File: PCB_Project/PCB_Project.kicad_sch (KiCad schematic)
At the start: 0 parts

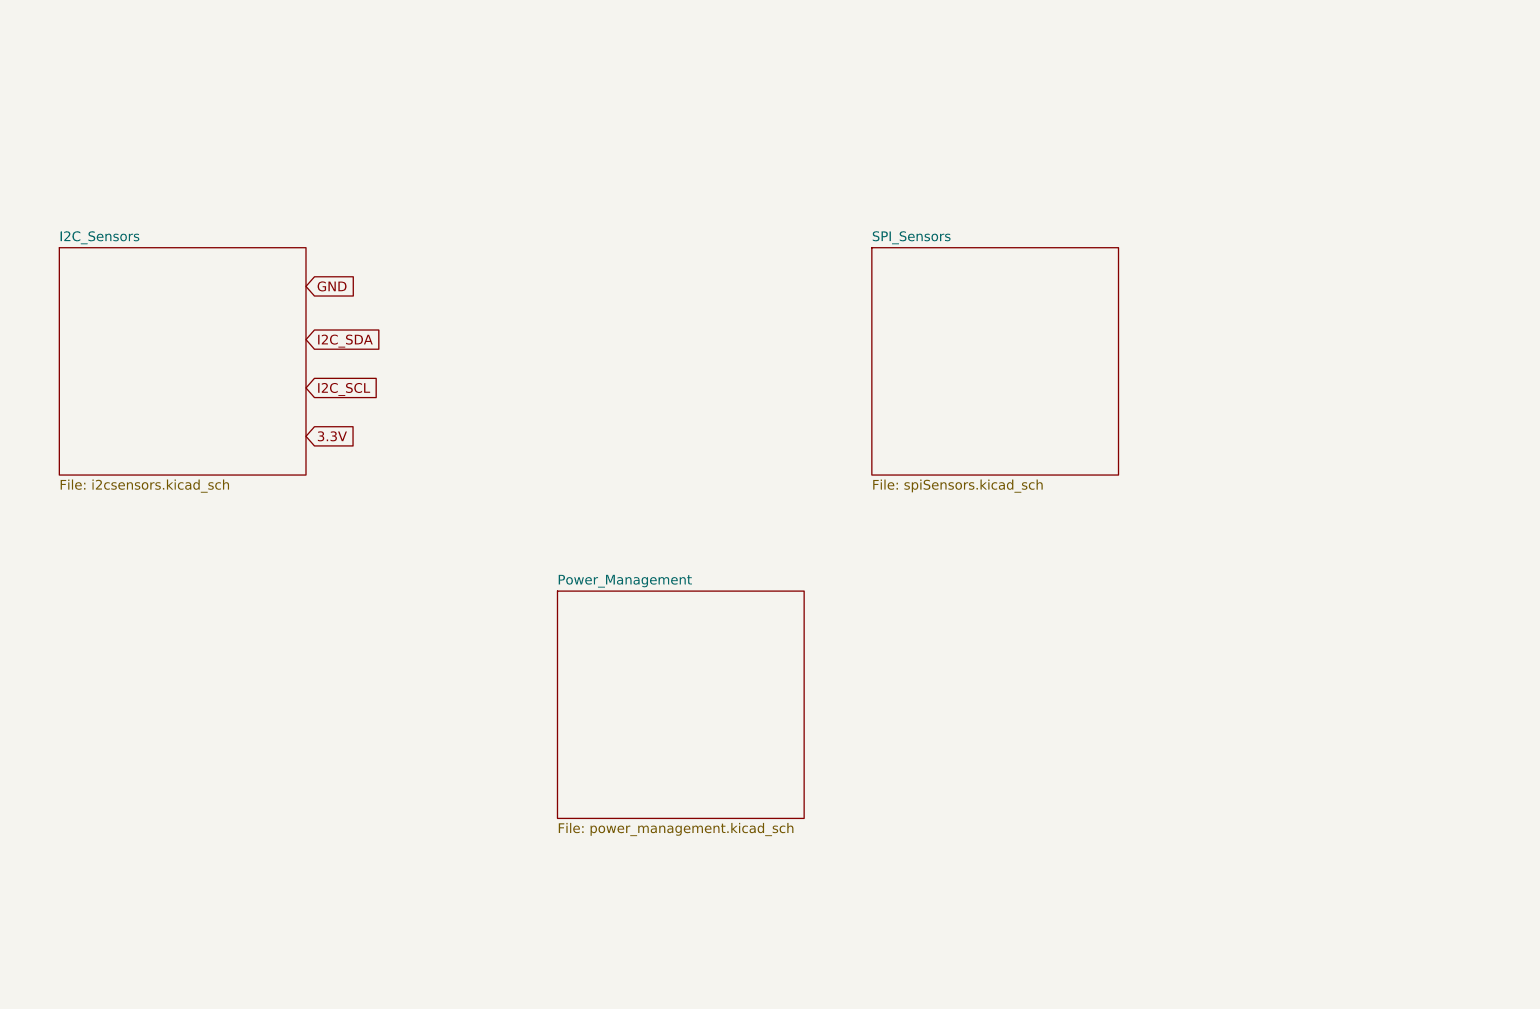
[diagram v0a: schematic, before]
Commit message: added raspberry pi connector
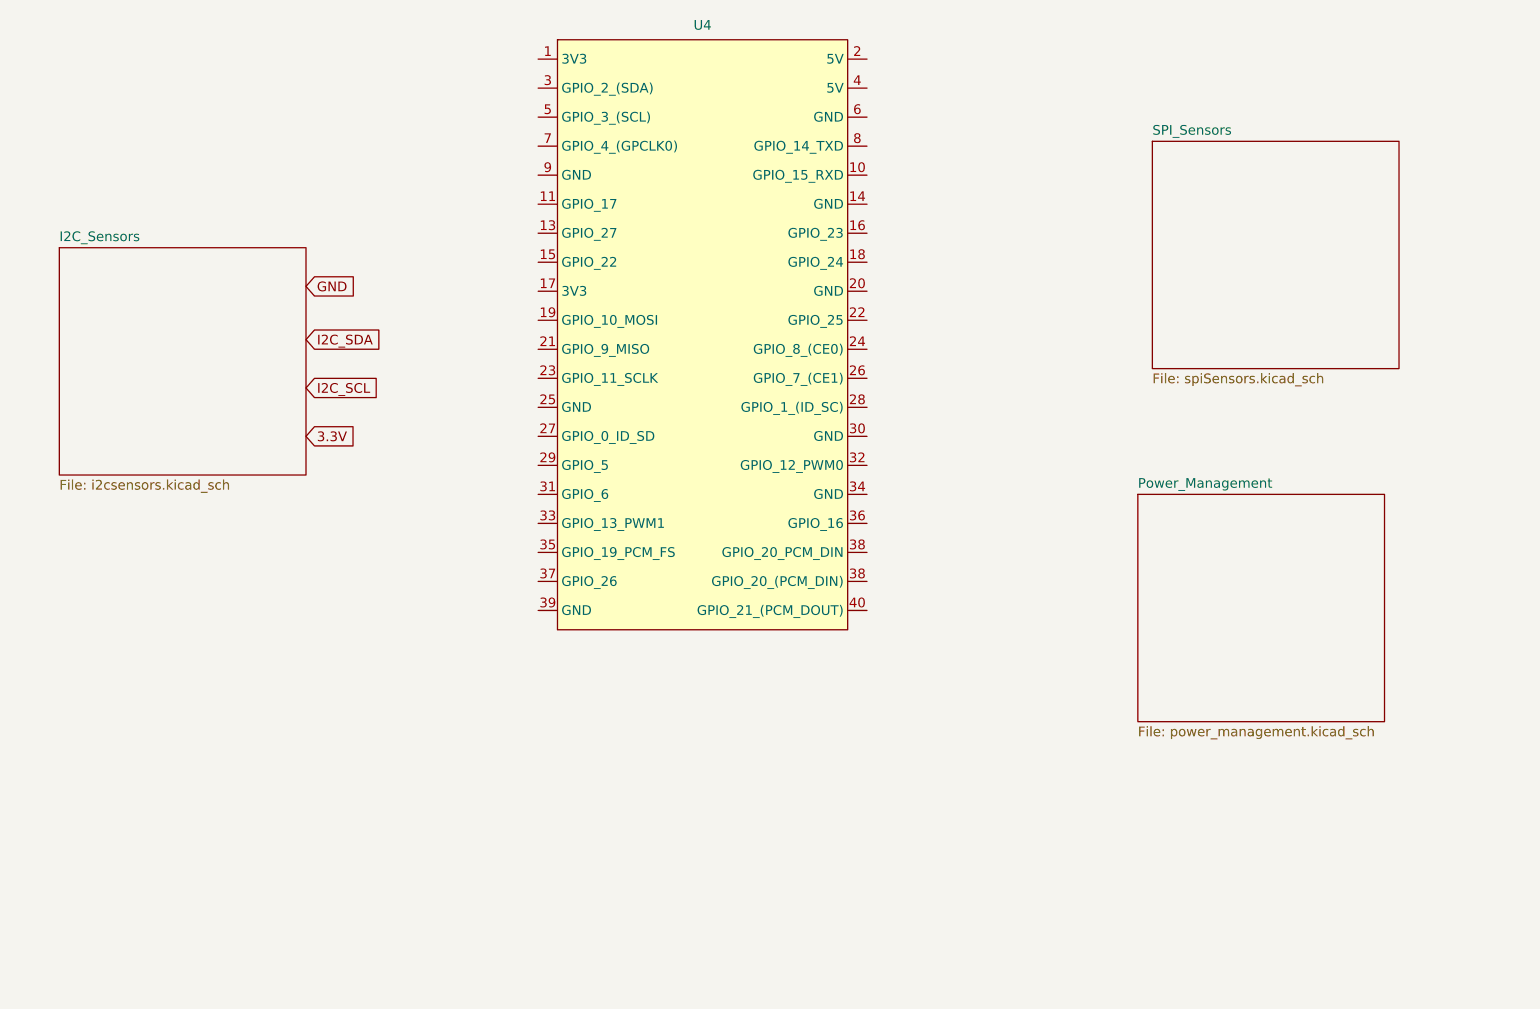
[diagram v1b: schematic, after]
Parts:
- added U4: ~, symbol Connector:Raspberry_Pi_5
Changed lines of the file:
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@@
+    )
+  )
+  (symbol (lib_id "Connector:Raspberry_Pi_5") (at 137.16 26.035 0) (unit 1)
+    (in_bom yes) (on_board yes) (dnp no) (fields_autoplaced)
+    (property "Reference" "U4" (at 137.16 22.86 0)
+      (effects (font (size 1.27 1.27)))
+    )
+    (property "Value" "~" (at 120.65 26.035 0)
+      (effects (font (size 1.27 1.27)))
+    )
+    (property "Footprint" "" (at 120.65 26.035 0)
+      (effects (font (size 1.27 1.27)) hide)
+    )
+    (property "Datasheet" "" (at 120.65 26.035 0)
+      (effects (font (size 1.27 1.27)) hide)
+    )
+    (pin "1")
+    (pin "10")
+    (pin "11")
+    (pin "13")
+    (pin "14")
+    (pin "15")
+    (pin "16")
+    (pin "17")
+    (pin "18")
+    (pin "19")
+    (pin "2")
+    (pin "20")
+    (pin "21")
+    (pin "22")
+    (pin "23")
+    (pin "24")
+    (pin "25")
+    (pin "26")
+    (pin "27")
+    (pin "28")
+    (pin "29")
+    (pin "3")
+    (pin "30")
+    (pin "31")
+    (pin "32")
+    (pin "33")
+    (pin "34")
+    (pin "35")
+    (pin "36")
+    (pin "37")
+    (pin "38")
+    (pin "38")
+    (pin "39")
+    (pin "4")
+    (pin "40")
+    (pin "5")
+    (pin "6")
+    (pin "7")
+    (pin "8")
+    (pin "9")
+    (instances
+      (project "PCB_Project"
+        (path "/3dbd20c6-0b48-4a74-89bd-dd4c54711bfb"
+          (reference "U4") (unit 1)
+        )
+      )
     )
   )
@@
     )
   )
-  (sheet (at 159.385 52.07) (size 32.385 29.845) (fields_autoplaced)
+  (sheet (at 196.215 38.1) (size 32.385 29.845) (fields_autoplaced)
     (stroke (width 0.1524) (type solid))
     (fill (color 0 0 0 0.0000))
-    (property "Sheetname" "SPI_Sensors" (at 159.385 51.3584 0)
+    (property "Sheetname" "SPI_Sensors" (at 196.215 37.3884 0)
       (effects (font (size 1.27 1.27)) (justify left bottom))
     )
-    (property "Sheetfile" "spiSensors.kicad_sch" (at 159.385 82.4996 0)
+    (property "Sheetfile" "spiSensors.kicad_sch" (at 196.215 68.5296 0)
       (effects (font (size 1.27 1.27)) (justify left top))
     )
@@
     )
   )
-  (sheet (at 118.11 97.155) (size 32.385 29.845) (fields_autoplaced)
+  (sheet (at 194.31 84.455) (size 32.385 29.845) (fields_autoplaced)
     (stroke (width 0.1524) (type solid))
     (fill (color 0 0 0 0.0000))
-    (property "Sheetname" "Power_Management" (at 118.11 96.4434 0)
+    (property "Sheetname" "Power_Management" (at 194.31 83.7434 0)
       (effects (font (size 1.27 1.27)) (justify left bottom))
     )
-    (property "Sheetfile" "power_management.kicad_sch" (at 118.11 127.5846 0)
+    (property "Sheetfile" "power_management.kicad_sch" (at 194.31 114.8846 0)
       (effects (font (size 1.27 1.27)) (justify left top))
     )

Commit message: cleanup
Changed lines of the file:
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@@
     )
   )
-  (sheet (at 196.215 38.1) (size 32.385 29.845) (fields_autoplaced)
+  (sheet (at 205.105 37.465) (size 32.385 29.845) (fields_autoplaced)
     (stroke (width 0.1524) (type solid))
     (fill (color 0 0 0 0.0000))
-    (property "Sheetname" "SPI_Sensors" (at 196.215 37.3884 0)
+    (property "Sheetname" "SPI_Sensors" (at 205.105 36.7534 0)
       (effects (font (size 1.27 1.27)) (justify left bottom))
     )
-    (property "Sheetfile" "spiSensors.kicad_sch" (at 196.215 68.5296 0)
+    (property "Sheetfile" "spiSensors.kicad_sch" (at 205.105 67.8946 0)
       (effects (font (size 1.27 1.27)) (justify left top))
     )
@@
     )
   )
-  (sheet (at 194.31 84.455) (size 32.385 29.845) (fields_autoplaced)
+  (sheet (at 205.105 79.375) (size 32.385 29.845) (fields_autoplaced)
     (stroke (width 0.1524) (type solid))
     (fill (color 0 0 0 0.0000))
-    (property "Sheetname" "Power_Management" (at 194.31 83.7434 0)
+    (property "Sheetname" "Power_Management" (at 205.105 78.6634 0)
       (effects (font (size 1.27 1.27)) (justify left bottom))
     )
-    (property "Sheetfile" "power_management.kicad_sch" (at 194.31 114.8846 0)
+    (property "Sheetfile" "power_management.kicad_sch" (at 205.105 109.8046 0)
       (effects (font (size 1.27 1.27)) (justify left top))
     )

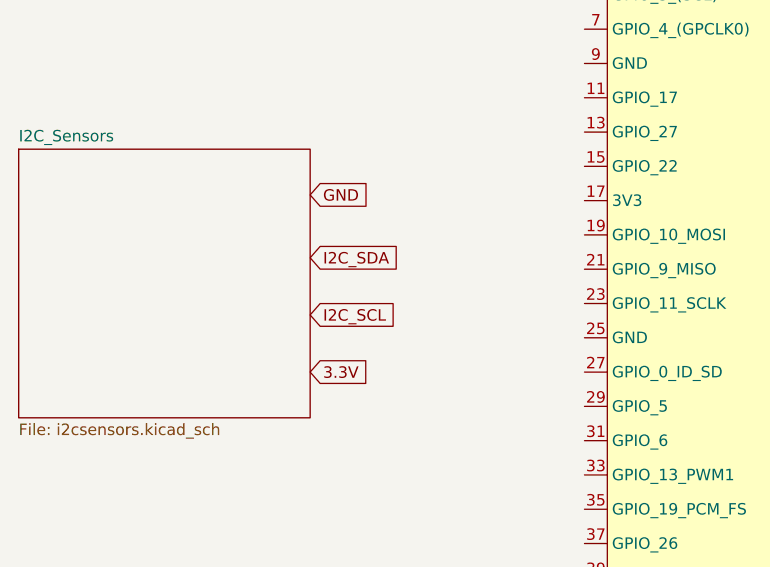
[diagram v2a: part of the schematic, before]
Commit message: added power board
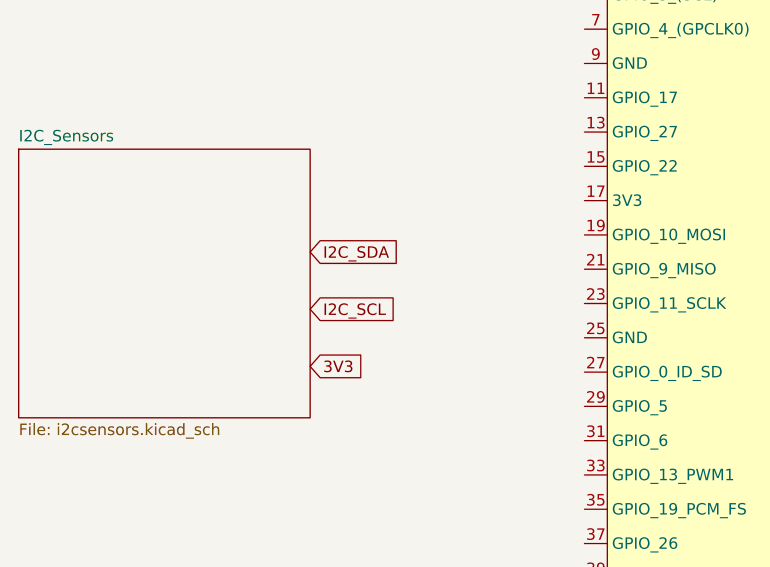
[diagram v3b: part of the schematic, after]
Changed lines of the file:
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@@
 (kicad_sch (version 20230121) (generator eeschema)
   (paper "A4")
-  (global_label "I2C_SCL" (shape input) (at 85.09 70.485 0) (fields_autoplaced)
+  (global_label "I2C_SCL" (shape input) (at 85.09 69.85 0) (fields_autoplaced)
     (effects (font (size 1.27 1.27)) (justify left))
-    (property "Intersheetrefs" "${INTERSHEET_REFS}" (at 95.5553 70.485 0)
+    (property "Intersheetrefs" "${INTERSHEET_REFS}" (at 95.5553 69.85 0)
       (effects (font (size 1.27 1.27)) (justify left) hide)
     )
   )
-  (global_label "I2C_SDA" (shape input) (at 85.09 64.135 0) (fields_autoplaced)
+  (global_label "I2C_SDA" (shape input) (at 85.09 63.5 0) (fields_autoplaced)
     (effects (font (size 1.27 1.27)) (justify left))
-    (property "Intersheetrefs" "${INTERSHEET_REFS}" (at 95.6158 64.135 0)
+    (property "Intersheetrefs" "${INTERSHEET_REFS}" (at 95.6158 63.5 0)
       (effects (font (size 1.27 1.27)) (justify left) hide)
     )
   )
-  (global_label "3.3V" (shape input) (at 85.09 76.835 0) (fields_autoplaced)
+  (global_label "3V3" (shape input) (at 85.09 76.2 0) (fields_autoplaced)
     (effects (font (size 1.27 1.27)) (justify left))
-    (property "Intersheetrefs" "${INTERSHEET_REFS}" (at 92.1082 76.835 0)
+    (property "Intersheetrefs" "${INTERSHEET_REFS}" (at 91.5034 76.2 0)
       (effects (font (size 1.27 1.27)) (justify left) hide)
     )
-  )
-  (global_label "GND" (shape input) (at 85.09 57.15 0) (fields_autoplaced)
-    (effects (font (size 1.27 1.27)) (justify left))
-    (property "Intersheetrefs" "${INTERSHEET_REFS}" (at 91.8663 57.15 0)
-      (effects (font (size 1.27 1.27)) (justify left) hide)
-    )

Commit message: clean up thx david!
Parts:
- U4: footprint (none) -> Connector_PinHeader_2.54mm:PinHeader_2x20_P2.54mm_Vertical
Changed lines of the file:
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@@
       (effects (font (size 1.27 1.27)))
     )
-    (property "Footprint" "" (at 120.65 26.035 0)
+    (property "Footprint" "Connector_PinHeader_2.54mm:PinHeader_2x20_P2.54mm_Vertical" (at 120.65 26.035 0)
       (effects (font (size 1.27 1.27)) hide)
     )

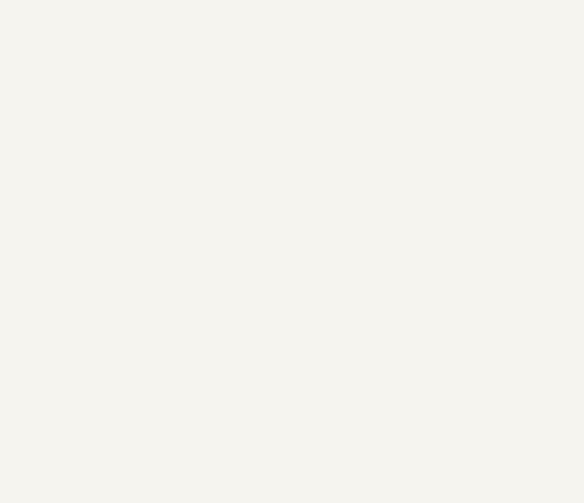
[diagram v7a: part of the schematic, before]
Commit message: motor driver started
address is 5C
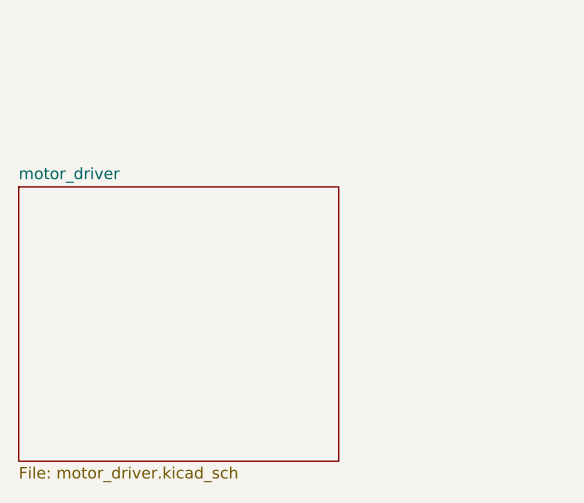
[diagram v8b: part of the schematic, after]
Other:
- added sheet motor_driver (motor_driver.kicad_sch)
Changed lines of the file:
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@@
+    )
+  )
+  (sheet (at 46.99 116.84) (size 35.56 30.48) (fields_autoplaced)
+    (stroke (width 0.1524) (type solid))
+    (fill (color 0 0 0 0.0000))
+    (property "Sheetname" "motor_driver" (at 46.99 116.1284 0)
+      (effects (font (size 1.27 1.27)) (justify left bottom))
+    )
+    (property "Sheetfile" "motor_driver.kicad_sch" (at 46.99 147.9046 0)
+      (effects (font (size 1.27 1.27)) (justify left top))
+    )
+    (instances
+      (project "PCB_Project"
+        (path "/3dbd20c6-0b48-4a74-89bd-dd4c54711bfb" (page "5"))
+      )
     )
   )
